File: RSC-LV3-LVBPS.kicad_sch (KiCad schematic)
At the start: 3 parts, among them J5 Conn_01x02, SW1 SW_SPST

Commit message: more schematic work and initial layout
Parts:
- added C28: 100u, Capacitor_THT:CP_Radial_D6.3mm_P2.50mm, symbol Device:C_Polarized
- added J6: Conn_01x02, Connector_Molex:Molex_Micro-Fit_3.0_43650-0200_1x02_P3.00mm_Horizontal, symbol Connector_Generic:Conn_01x02
- added SW2: SLW-864587-2A-RA-N-D, SamacSys_Parts:SLW8645872ARAND, symbol Switch:SW_SPST
- SW1: value SW_SPST -> Molex 43650-0215; footprint Connector_Molex:Molex_Micro-Fit_3.0_43650-0215_1x02_P3.00mm_Vertical -> Connector_Molex:Molex_Micro-Fit_3.0_43650-0200_1x02_P3.00mm_Horizontal
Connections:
- net +12V_DCDC: now also J6.2 (Pin_2)
- net +12V_LOCAL: now also SW2.2 (A)
- net Current Sense (BAT)/OUT: now also SW2.3 (B)
- net Current Sense (LOAD)/IN: now also C28.1
- net GND: now also C28.2, J6.1 (Pin_1)
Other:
- added sheet Precharge (Precharge.kicad_sch)
- moved on the sheet: SW1

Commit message: more layout work
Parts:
- removed SW1: Molex 43650-0215, Connector_Molex:Molex_Micro-Fit_3.0_43650-0200_1x02_P3.00mm_Horizontal, symbol Switch:SW_SPST
- added C36: 1u, Capacitor_SMD:C_0603_1608Metric_Pad1.08x0.95mm_HandSolder, symbol Device:C
- added J7: Conn_01x02, Connector_Molex:Molex_Micro-Fit_3.0_43650-0200_1x02_P3.00mm_Horizontal, symbol Connector_Generic:Conn_01x02
- added J8: Molex 43045-0400, Connector_Molex:Molex_Micro-Fit_3.0_43045-0400_2x02_P3.00mm_Horizontal, symbol Connector_Generic:Conn_02x02_Top_Bottom
- added Q3: AO3400A, Package_TO_SOT_SMD:SOT-23, symbol Transistor_FET:AO3400A
- added R32: 10k, Resistor_SMD:R_0603_1608Metric_Pad0.98x0.95mm_HandSolder, symbol Device:R
- added R33: 1k, Resistor_SMD:R_0603_1608Metric_Pad0.98x0.95mm_HandSolder, symbol Device:R
- added R34: 5.1k, Resistor_SMD:R_0603_1608Metric_Pad0.98x0.95mm_HandSolder, symbol Device:R
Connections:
- net +12V_LOCAL: now also J8.2 (Pin_2), J8.3 (Pin_3)
- net Current Sense (BAT)/OUT: now also J8.1 (Pin_1)
- net GND: now also C36.2, J7.1 (Pin_1), Q3.2 (S), R34.2
- new net: J8.4 (Pin_4), Q3.3 (D)
- new net: J7.2 (Pin_2), R32.2, R33.2
- new net +3.3V: R32.1
- new net POWER_SWITCH_LED: Q3.1 (G), R34.1
- new net THERMISTOR_SENSE: C36.1, R33.1
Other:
- moved on the sheet: SW2

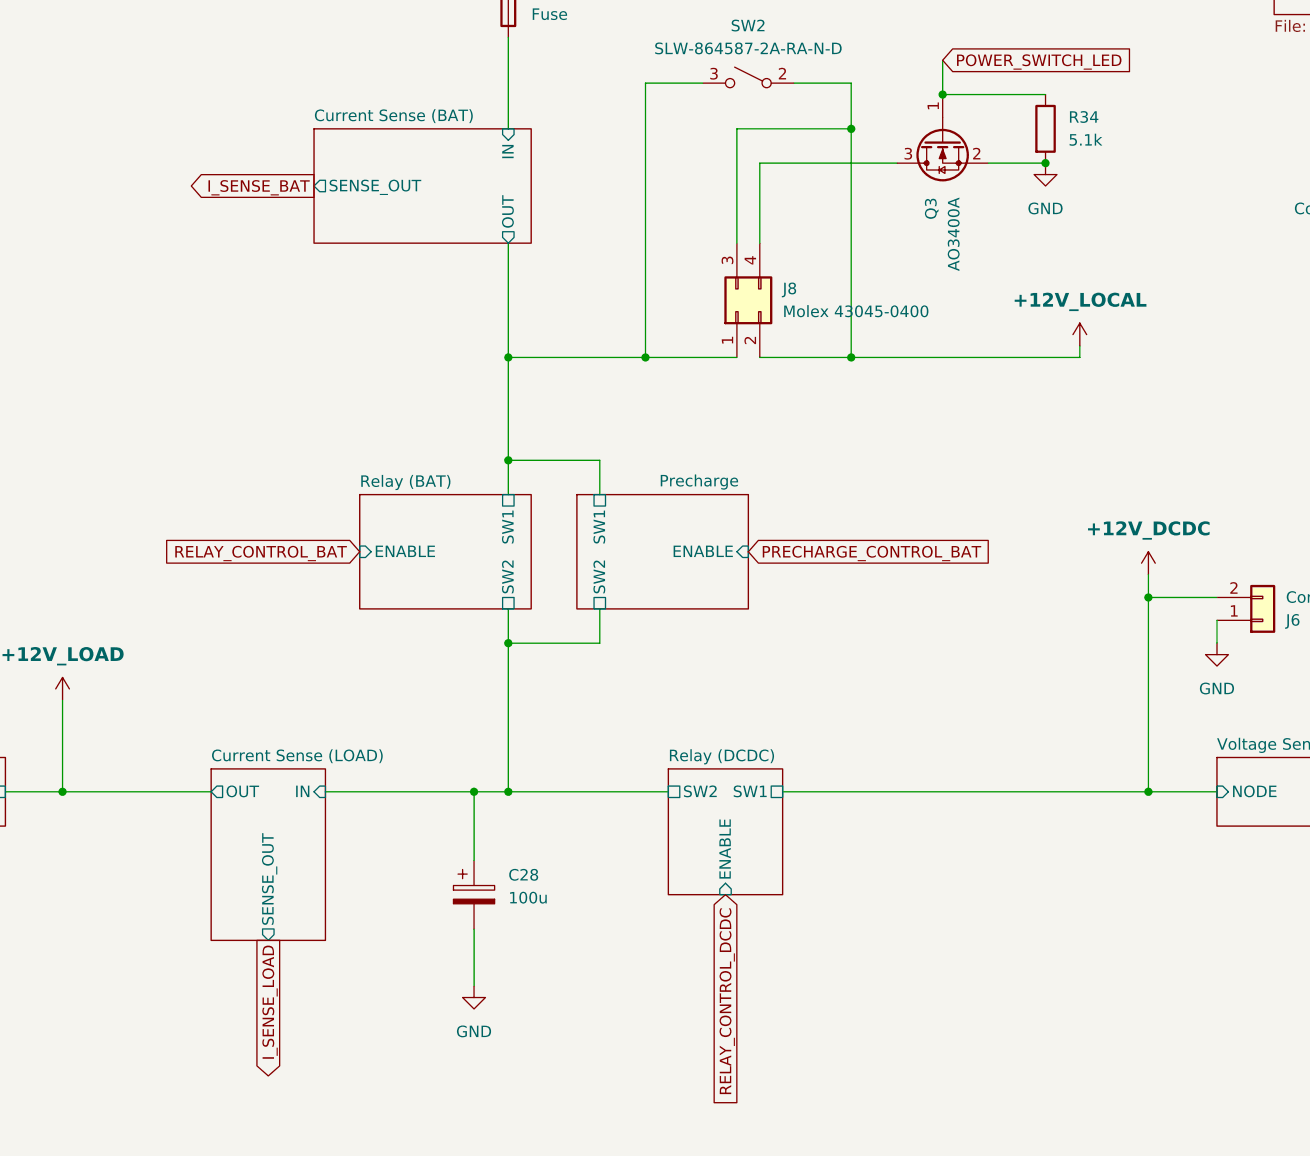
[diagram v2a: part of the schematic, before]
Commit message: schematic changes and initial routing
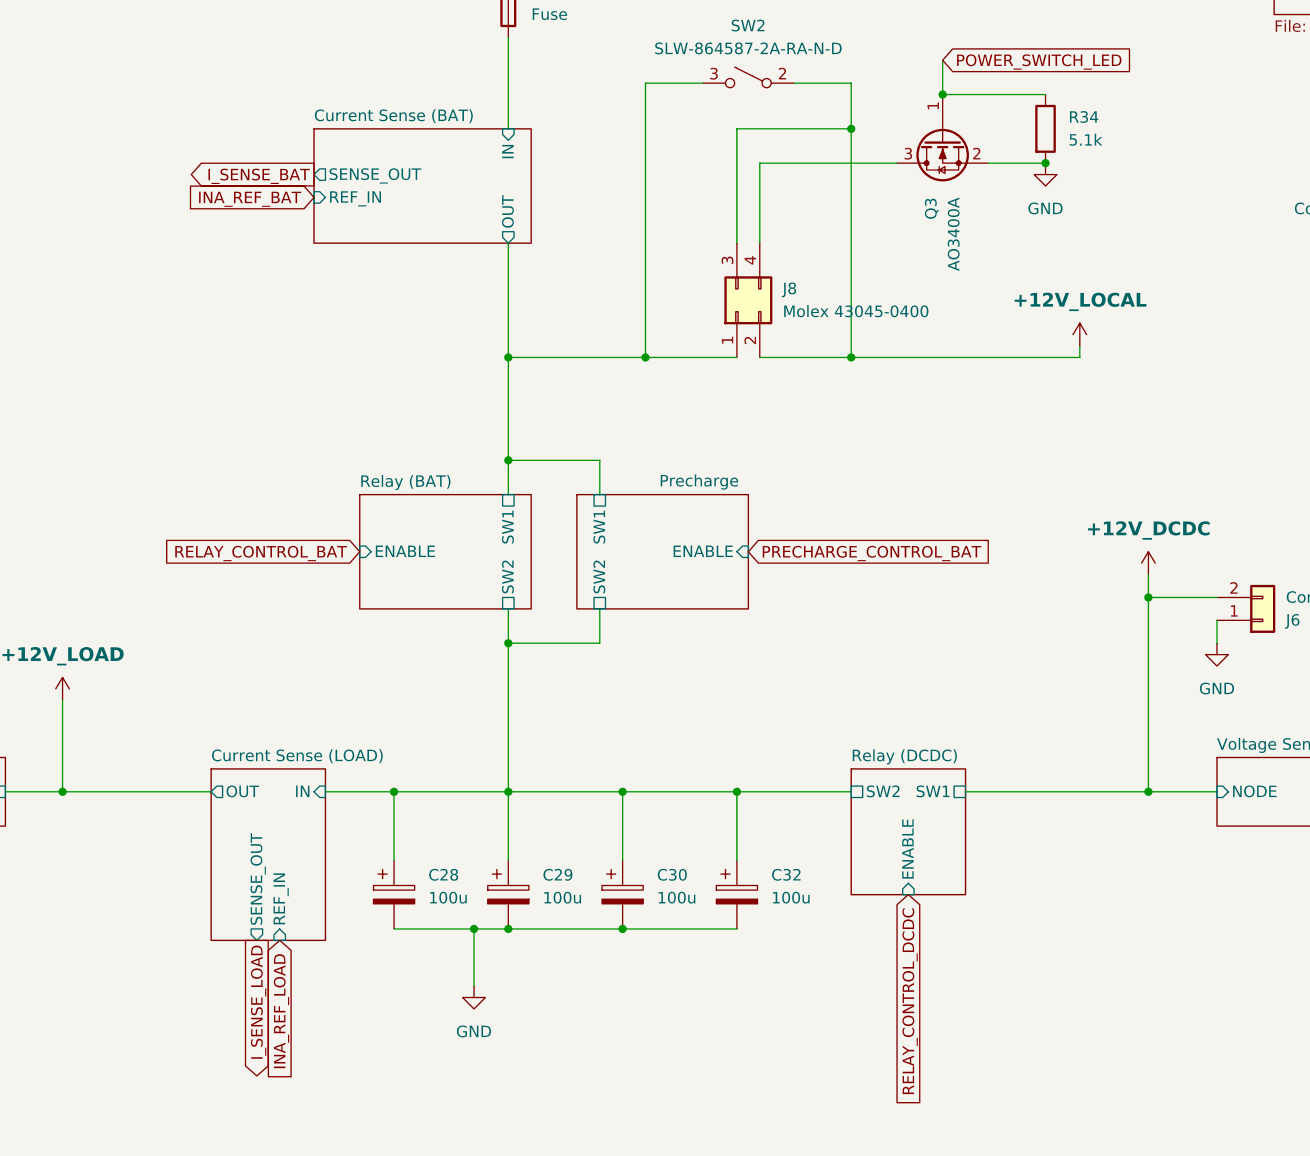
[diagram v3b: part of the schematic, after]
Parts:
- added C29, C30, C32: 100u, Capacitor_THT:CP_Radial_D6.3mm_P2.50mm, symbol Device:C_Polarized
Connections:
- net Current Sense (LOAD)/IN: now also C29.1, C30.1, C32.1
- net GND: now also C29.2, C30.2, C32.2
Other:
- sheet Current Sense (BAT) ports: added REF_IN; removed none
- sheet Current Sense (LOAD) ports: added REF_IN; removed none
- moved on the sheet: C28

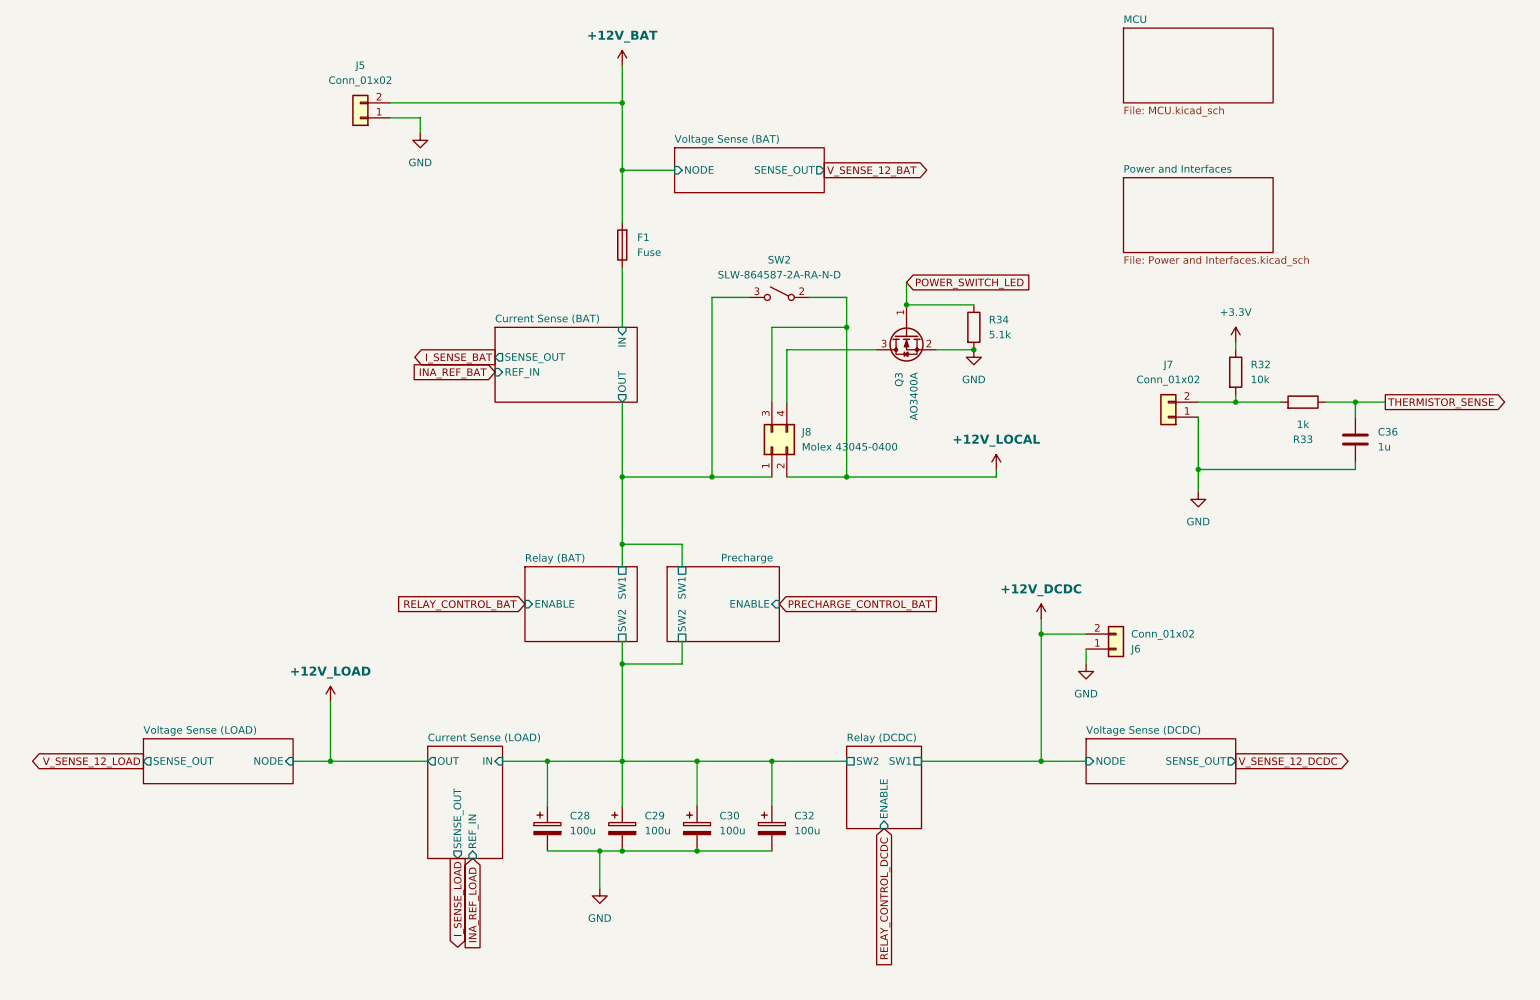
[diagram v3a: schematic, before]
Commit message: finished layout, routing, and silkscreen
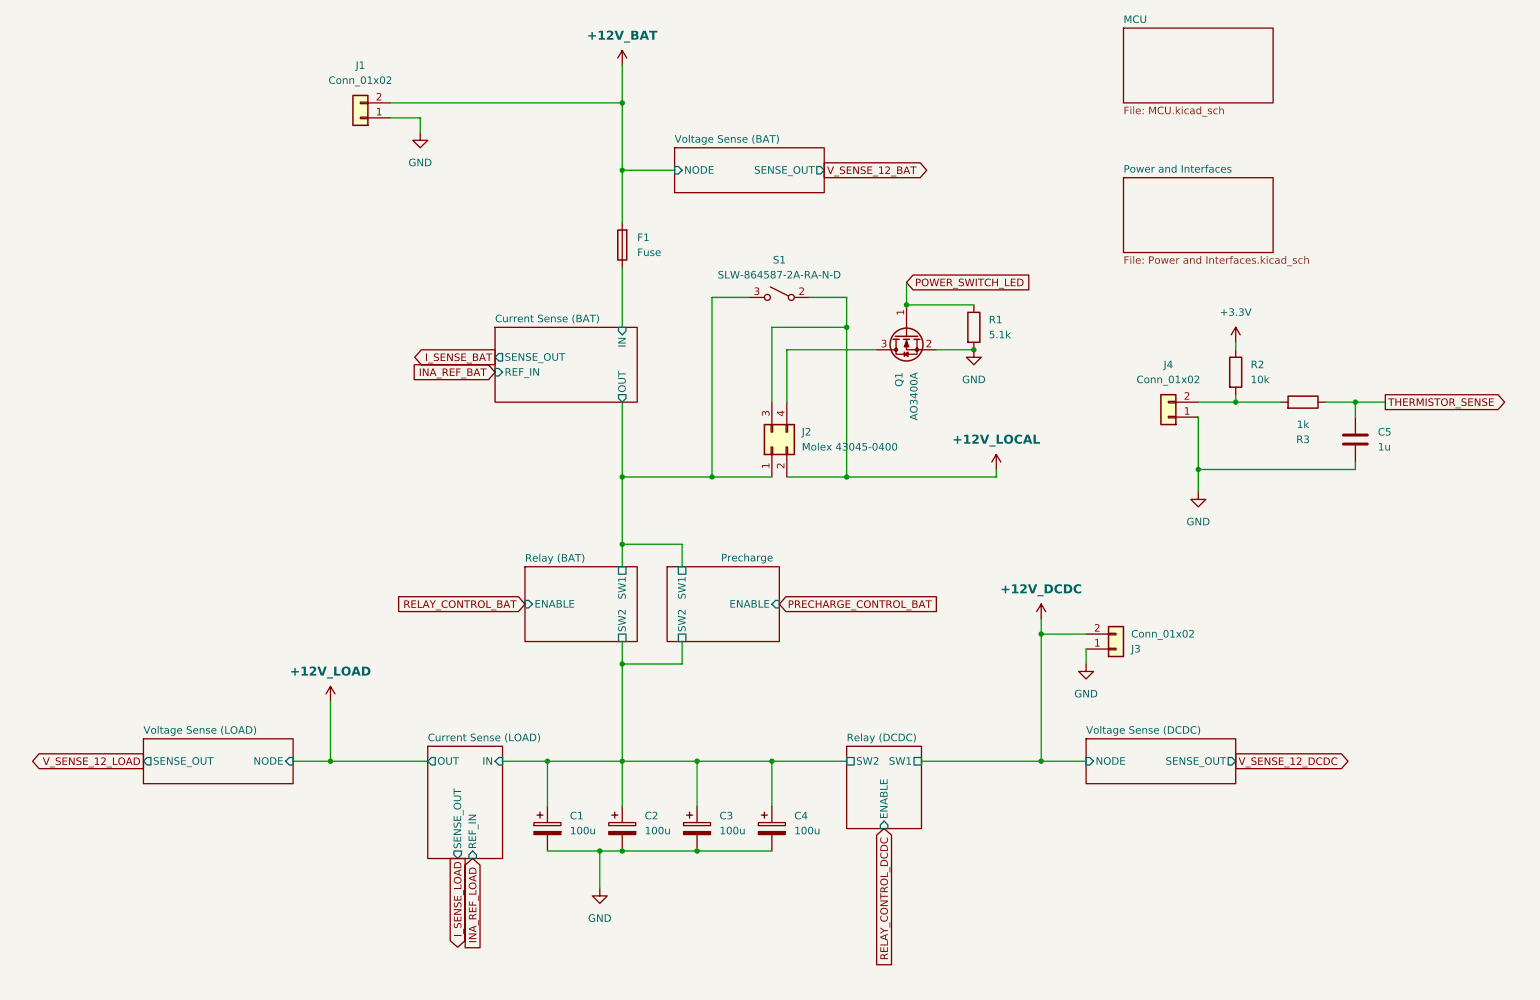
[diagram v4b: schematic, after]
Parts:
- renumbered C28 to C1, C29 to C2, C30 to C3, C32 to C4, C36 to C5, J5 to J1, J8 to J2, J6 to J3, J7 to J4, Q3 to Q1, R34 to R1, R32 to R2, R33 to R3, SW2 to S1
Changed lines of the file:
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@@
 		(in_pos_files yes)
 		(dnp no)
-		(property "Reference" "Q3"
+		(property "Reference" "Q1"
 			(at 170.1799 83.82 0)
 			(show_name no)
@@
 			(project "RSC-LV3-LVBPS"
 				(path "/4bbf2fff-9f66-421d-84bf-68d1dcd1e11d"
-					(reference "Q3")
+					(reference "Q1")
 					(unit 1)
 				)
@@
 		(dnp no)
 		(fields_autoplaced yes)
-		(property "Reference" "#PWR067"
+		(property "Reference" "#PWR010"
 			(at 227.33 82.55 0)
 			(hide yes)
@@
 			(project "RSC-LV3-LVBPS"
 				(path "/4bbf2fff-9f66-421d-84bf-68d1dcd1e11d"
-					(reference "#PWR067")
+					(reference "#PWR010")
 					(unit 1)
 				)
@@
 		(dnp no)
 		(fields_autoplaced yes)
-		(property "Reference" "R34"
+		(property "Reference" "R1"
 			(at 185.42 74.9299 0)
 			(show_name no)
@@
 			(project "RSC-LV3-LVBPS"
 				(path "/4bbf2fff-9f66-421d-84bf-68d1dcd1e11d"
-					(reference "R34")
+					(reference "R1")
 					(unit 1)
 				)
@@
 		(dnp no)
 		(fields_autoplaced yes)
-		(property "Reference" "#PWR03"
+		(property "Reference" "#PWR01"
 			(at 73.66 143.51 0)
 			(hide yes)
@@
 			(project "RSC-LV3-LVBPS"
 				(path "/4bbf2fff-9f66-421d-84bf-68d1dcd1e11d"
-					(reference "#PWR03")
+					(reference "#PWR01")
 					(unit 1)
 				)
@@
 		(dnp no)
 		(fields_autoplaced yes)
-		(property "Reference" "#PWR068"
+		(property "Reference" "#PWR09"
 			(at 220.98 110.49 0)
 			(hide yes)
@@
 			(project "RSC-LV3-LVBPS"
 				(path "/4bbf2fff-9f66-421d-84bf-68d1dcd1e11d"
-					(reference "#PWR068")
+					(reference "#PWR09")
 					(unit 1)
 				)
@@
 		(dnp no)
 		(fields_autoplaced yes)
-		(property "Reference" "J5"
+		(property "Reference" "J1"
 			(at 78.74 31.75 0)
 			(show_name no)
@@
 			(project "RSC-LV3-LVBPS"
 				(path "/4bbf2fff-9f66-421d-84bf-68d1dcd1e11d"
-					(reference "J5")
+					(reference "J1")
 					(unit 1)
 				)
@@
 		(dnp no)
 		(fields_autoplaced yes)
-		(property "Reference" "J8"
+		(property "Reference" "J2"
 			(at 153.67 93.9799 90)
 			(show_name no)
@@
 			(project "RSC-LV3-LVBPS"
 				(path "/4bbf2fff-9f66-421d-84bf-68d1dcd1e11d"
-					(reference "J8")
+					(reference "J2")
 					(unit 1)
 				)
@@
 		(dnp no)
 		(fields_autoplaced yes)
-		(property "Reference" "R32"
+		(property "Reference" "R2"
 			(at 229.87 82.5499 0)
 			(show_name no)
@@
 			(project "RSC-LV3-LVBPS"
 				(path "/4bbf2fff-9f66-421d-84bf-68d1dcd1e11d"
-					(reference "R32")
+					(reference "R2")
 					(unit 1)
 				)
@@
 		(dnp no)
 		(fields_autoplaced yes)
-		(property "Reference" "SW2"
+		(property "Reference" "S1"
 			(at 149.86 64.77 0)
 			(show_name no)
@@
 			(project "RSC-LV3-LVBPS"
 				(path "/4bbf2fff-9f66-421d-84bf-68d1dcd1e11d"
-					(reference "SW2")
+					(reference "S1")
 					(unit 1)
 				)
@@
 		(dnp no)
 		(fields_autoplaced yes)
-		(property "Reference" "#PWR069"
+		(property "Reference" "#PWR05"
 			(at 182.88 86.36 0)
 			(hide yes)
@@
 			(project "RSC-LV3-LVBPS"
 				(path "/4bbf2fff-9f66-421d-84bf-68d1dcd1e11d"
-					(reference "#PWR069")
+					(reference "#PWR05")
 					(unit 1)
 				)
@@
 		(dnp no)
 		(fields_autoplaced yes)
-		(property "Reference" "C30"
+		(property "Reference" "C3"
 			(at 139.7 159.1309 0)
 			(show_name no)
@@
 			(project "RSC-LV3-LVBPS"
 				(path "/4bbf2fff-9f66-421d-84bf-68d1dcd1e11d"
-					(reference "C30")
+					(reference "C3")
 					(unit 1)
 				)
@@
 		(dnp no)
 		(fields_autoplaced yes)
-		(property "Reference" "#PWR01"
+		(property "Reference" "#PWR04"
 			(at 123.19 35.56 0)
 			(hide yes)
@@
 			(project "RSC-LV3-LVBPS"
 				(path "/4bbf2fff-9f66-421d-84bf-68d1dcd1e11d"
-					(reference "#PWR01")
+					(reference "#PWR04")
 					(unit 1)
 				)
@@
 		(dnp no)
 		(fields_autoplaced yes)
-		(property "Reference" "#PWR063"
+		(property "Reference" "#PWR02"
 			(at 88.9 49.53 0)
 			(hide yes)
@@
 			(project "RSC-LV3-LVBPS"
 				(path "/4bbf2fff-9f66-421d-84bf-68d1dcd1e11d"
-					(reference "#PWR063")
+					(reference "#PWR02")
 					(unit 1)
 				)
@@
 		(dnp no)
 		(fields_autoplaced yes)
-		(property "Reference" "#PWR02"
+		(property "Reference" "#PWR07"
 			(at 194.31 129.54 0)
 			(hide yes)
@@
 			(project "RSC-LV3-LVBPS"
 				(path "/4bbf2fff-9f66-421d-84bf-68d1dcd1e11d"
-					(reference "#PWR02")
+					(reference "#PWR07")
 					(unit 1)
 				)
@@
 		(dnp no)
 		(fields_autoplaced yes)
-		(property "Reference" "C36"
+		(property "Reference" "C5"
 			(at 251.46 93.9799 0)
 			(show_name no)
@@
 			(project "RSC-LV3-LVBPS"
 				(path "/4bbf2fff-9f66-421d-84bf-68d1dcd1e11d"
-					(reference "C36")
+					(reference "C5")
 					(unit 1)
 				)
@@
 		(dnp no)
 		(fields_autoplaced yes)
-		(property "Reference" "#PWR066"
+		(property "Reference" "#PWR08"
 			(at 201.93 139.7 0)
 			(hide yes)
@@
 			(project "RSC-LV3-LVBPS"
 				(path "/4bbf2fff-9f66-421d-84bf-68d1dcd1e11d"
-					(reference "#PWR066")
+					(reference "#PWR08")
 					(unit 1)
 				)
@@
 		(dnp no)
 		(fields_autoplaced yes)
-		(property "Reference" "#PWR04"
+		(property "Reference" "#PWR06"
 			(at 186.69 104.14 0)
 			(hide yes)
@@
 			(project "RSC-LV3-LVBPS"
 				(path "/4bbf2fff-9f66-421d-84bf-68d1dcd1e11d"
-					(reference "#PWR04")
+					(reference "#PWR06")
 					(unit 1)
 				)
@@
 		(dnp no)
 		(fields_autoplaced yes)
-		(property "Reference" "#PWR065"
+		(property "Reference" "#PWR03"
 			(at 119.38 177.8 0)
 			(hide yes)
@@
 			(project "RSC-LV3-LVBPS"
 				(path "/4bbf2fff-9f66-421d-84bf-68d1dcd1e11d"
-					(reference "#PWR065")
+					(reference "#PWR03")
 					(unit 1)
 				)
@@
 		(dnp no)
 		(fields_autoplaced yes)
-		(property "Reference" "C28"
+		(property "Reference" "C1"
 			(at 114.3 159.1309 0)
 			(show_name no)
@@
 			(project "RSC-LV3-LVBPS"
 				(path "/4bbf2fff-9f66-421d-84bf-68d1dcd1e11d"
-					(reference "C28")
+					(reference "C1")
 					(unit 1)
 				)
@@
 		(dnp no)
 		(fields_autoplaced yes)
-		(property "Reference" "C29"
+		(property "Reference" "C2"
 			(at 127 159.1309 0)
 			(show_name no)
@@
 			(project "RSC-LV3-LVBPS"
 				(path "/4bbf2fff-9f66-421d-84bf-68d1dcd1e11d"
-					(reference "C29")
+					(reference "C2")
 					(unit 1)
 				)
@@
 		(dnp no)
 		(fields_autoplaced yes)
-		(property "Reference" "C32"
+		(property "Reference" "C4"
 			(at 152.4 159.1309 0)
 			(show_name no)
@@
 			(project "RSC-LV3-LVBPS"
 				(path "/4bbf2fff-9f66-421d-84bf-68d1dcd1e11d"
-					(reference "C32")
+					(reference "C4")
 					(unit 1)
 				)
@@
 		(in_pos_files yes)
 		(dnp no)
-		(property "Reference" "J6"
+		(property "Reference" "J3"
 			(at 209.5836 130.8101 0)
 			(show_name no)
@@
 			(project "RSC-LV3-LVBPS"
 				(path "/4bbf2fff-9f66-421d-84bf-68d1dcd1e11d"
-					(reference "J6")
+					(reference "J3")
 					(unit 1)
 				)
@@
 		(in_pos_files yes)
 		(dnp no)
-		(property "Reference" "R33"
+		(property "Reference" "R3"
 			(at 238.76 95.25 90)
 			(show_name no)
@@
 			(project "RSC-LV3-LVBPS"
 				(path "/4bbf2fff-9f66-421d-84bf-68d1dcd1e11d"
-					(reference "R33")
+					(reference "R3")
 					(unit 1)
 				)
@@
 		(dnp no)
 		(fields_autoplaced yes)
-		(property "Reference" "J7"
+		(property "Reference" "J4"
 			(at 215.9 82.55 0)
 			(show_name no)
@@
 			(project "RSC-LV3-LVBPS"
 				(path "/4bbf2fff-9f66-421d-84bf-68d1dcd1e11d"
-					(reference "J7")
-					(unit 1)
-				)
+					(reference "J4")
+					(unit 1)
+				)
